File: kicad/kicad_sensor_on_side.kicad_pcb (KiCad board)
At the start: 2 copper layers, 33.9 x 42.5 mm, 12 parts, among them SW1 SW_Push, SW2 SW_Push, U1 nice_nano, U2 GY-BNO08X, U3 SSD1306_OLED_042

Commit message: various fixes
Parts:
- removed REF** (x4): MountingHole_2mm, MountingHole:MountingHole_2mm
- moved BAT+1 3.81 mm to (194.5, 85.0)
- moved SW_POWER1 1.80 mm to (194.0, 48.0)
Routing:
- net Net-(BAT-1-Pin_1): track 39.8 -> 37.5 mm
- net Net-(SW_POWER1-B): track 2.18 -> 2.85 mm
- net (no net): track 0.50 -> 0.00 mm

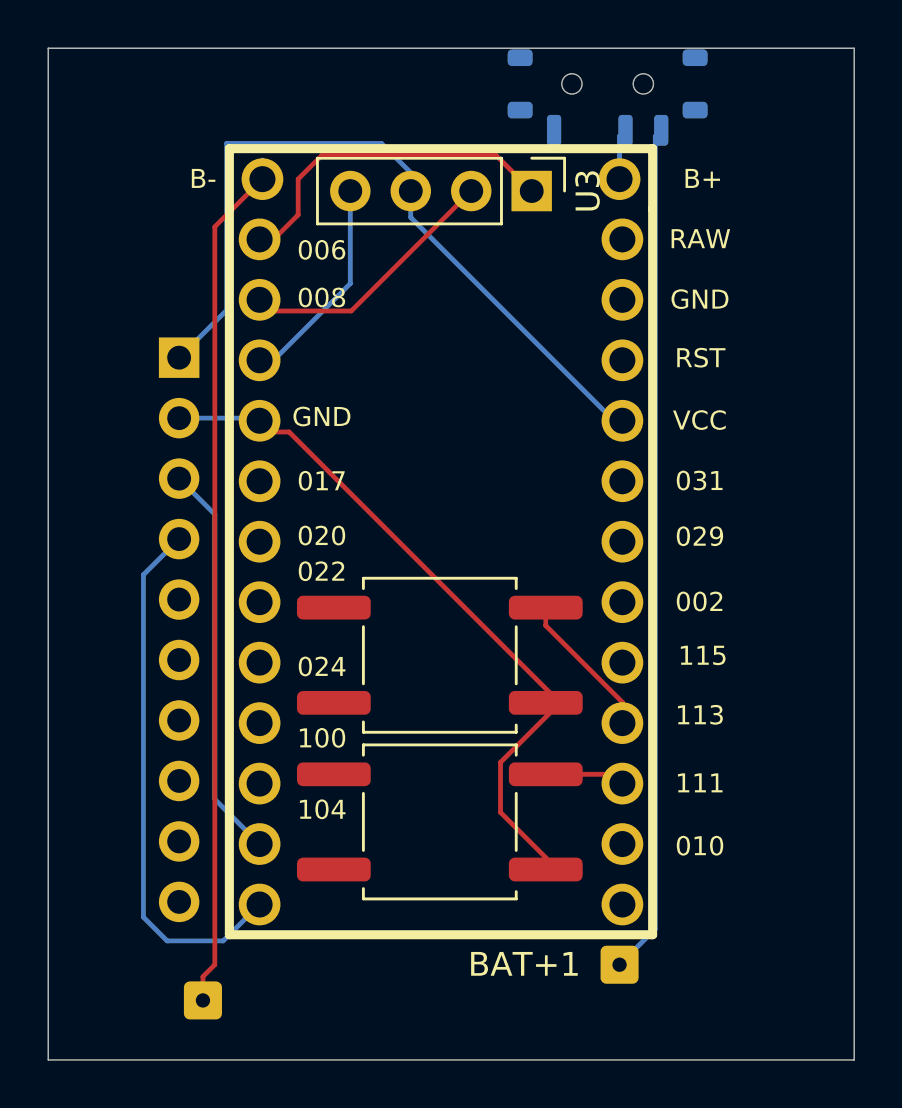
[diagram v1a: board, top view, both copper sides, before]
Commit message: thicker traces for battery in pcb
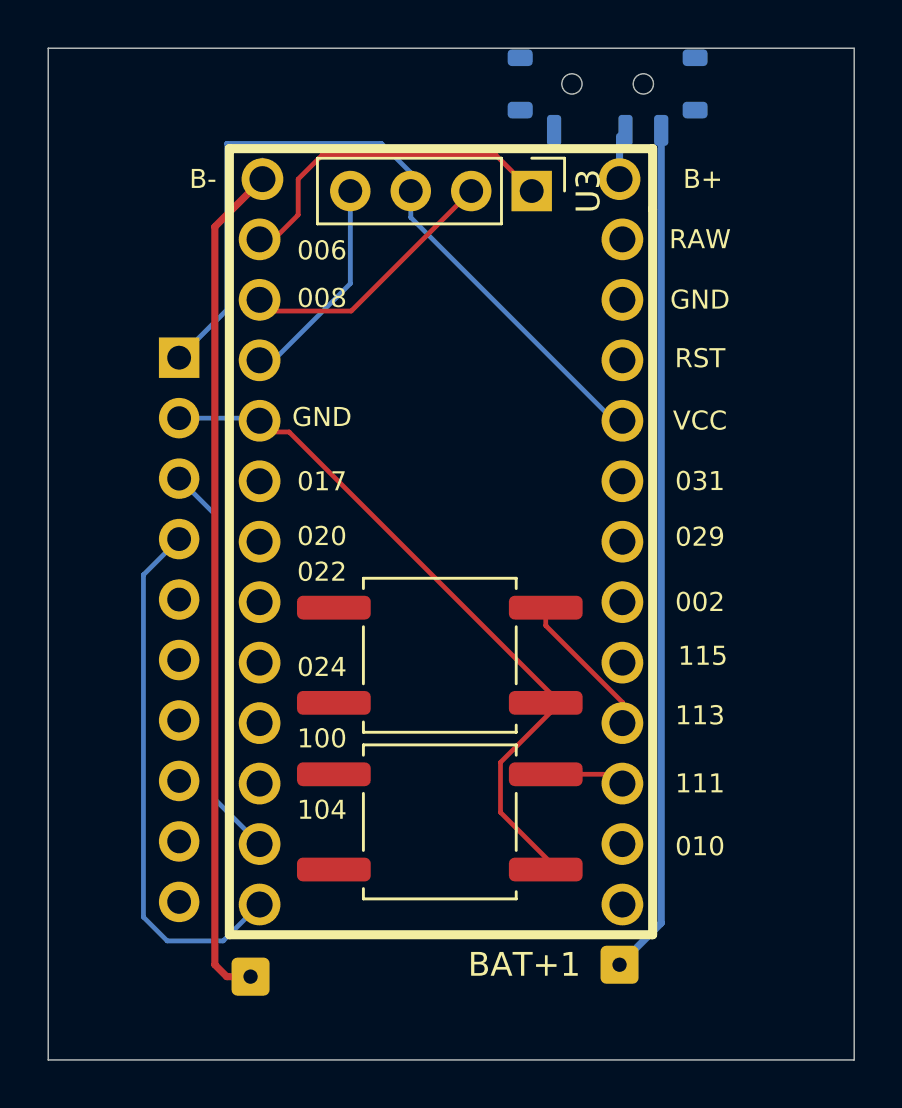
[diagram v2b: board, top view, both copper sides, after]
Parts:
- moved BAT-1 2.24 mm to (179.0, 85.5)
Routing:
- net Net-(BAT+1-Pin_1): track 35.8 -> 35.3 mm
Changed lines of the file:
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@@
 	(footprint "Connector_Wire:SolderWire-0.1sqmm_1x01_D0.4mm_OD1mm"
 		(layer "B.Cu")
-		(at 177 86.5)
+		(at 179 85.5)
 		(descr "Soldered wire connection, for a single 0.1 mm² wire, basic insulation, conductor diameter 0.4mm, outer diameter 1mm, size source Multi-Contact FLEXI-E 0.10 (https://www.staubli.com/content/dam/ecs/catalogs-brochures/TM/CAB-Main-11014119-en.pdf#page=9), bend radius 3 times outer diameter, generated with kicad-footprint-generator")
 		(tags "connector wire 0.1sqmm")
@@
 		(start 194.5 52)
 		(end 194.5 50.2)
-		(width 0.2)
+		(width 0.3)
 		(layer "B.Cu")
 		(net "Net-(SW_POWER1-B)")
@@
 		(start 177.5 85)
 		(end 177.5 54)
-		(width 0.2)
+		(width 0.3)
 		(layer "F.Cu")
 		(net "Net-(BAT-1-Pin_1)")
@@
 		(start 177.5 54)
 		(end 179.5 52)
-		(width 0.2)
+		(width 0.3)
 		(layer "F.Cu")
 		(net "Net-(BAT-1-Pin_1)")
 	)
 	(segment
-		(start 177 86.5)
-		(end 177 85.5)
-		(width 0.2)
+		(start 178 85.5)
+		(end 179 85.5)
+		(width 0.3)
 		(layer "F.Cu")
 		(net "Net-(BAT-1-Pin_1)")
 	)
 	(segment
-		(start 177 85.5)
-		(end 177.5 85)
-		(width 0.2)
+		(start 177.5 85)
+		(end 178 85.5)
+		(width 0.3)
 		(layer "F.Cu")
 		(net "Net-(BAT-1-Pin_1)")
@@
 	)
 	(segment
-		(start 196 83.5)
-		(end 196 50.2)
-		(width 0.2)
+		(start 194.5 85)
+		(end 196.25 83.25)
+		(width 0.3)
 		(layer "B.Cu")
 		(net "Net-(BAT+1-Pin_1)")
 	)
 	(segment
-		(start 196 50.2)
-		(end 196.25 49.95)
-		(width 0.2)
+		(start 196.25 83.25)
+		(end 196.25 50.45)
+		(width 0.3)
 		(layer "B.Cu")
 		(net "Net-(BAT+1-Pin_1)")
-	)
-	(segment
-		(start 194.5 85)
-		(end 196 83.5)
-		(width 0.2)
-		(layer "B.Cu")
-		(net "Net-(BAT+1-Pin_1)")
